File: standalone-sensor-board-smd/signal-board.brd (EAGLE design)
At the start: 26 x 93.5 mm, 27 parts, among them IC2 HEF4051BT,653, J1 sensors, J3 to_next_board, J4 to_controller

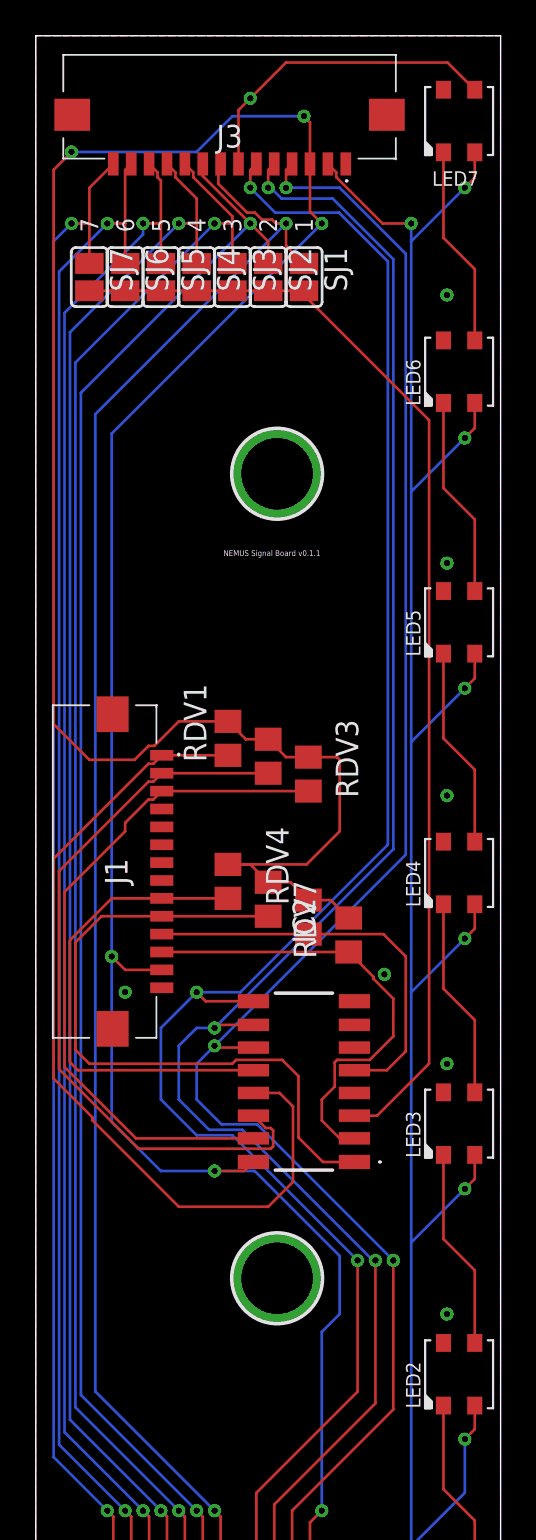
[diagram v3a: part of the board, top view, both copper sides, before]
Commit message: tidy silk screen
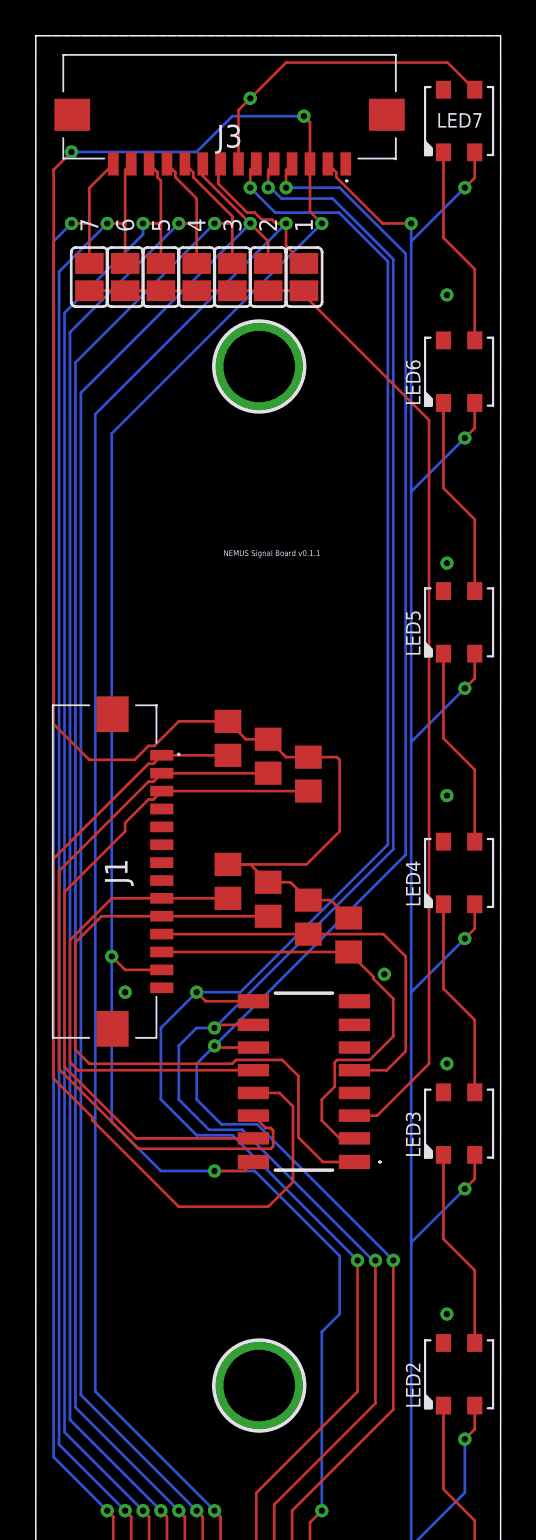
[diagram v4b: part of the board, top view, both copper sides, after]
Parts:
- moved U$1 6.08 mm to (12.5, 75.0)
- moved U$2 6.08 mm to (12.5, 18.0)
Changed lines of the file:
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@@
 <elements>
 <element name="SJ1" library="jumper" library_urn="urn:adsk.eagle:library:252" package="SJ" package3d_urn="urn:adsk.eagle:package:15471/1" value="" x="15" y="80" smashed="yes" rot="R270">
-<attribute name="NAME" x="16.143" y="81.651" size="1.27" layer="25" ratio="10" rot="R270"/>
 <attribute name="POPULARITY" value="33" x="15" y="80" size="1.778" layer="27" rot="R270" display="off"/>
 <attribute name="VALUE" x="15" y="79.5999" size="0.02" layer="27" rot="R270"/>
 </element>
 <element name="SJ2" library="jumper" library_urn="urn:adsk.eagle:library:252" package="SJ" package3d_urn="urn:adsk.eagle:package:15471/1" value="" x="13" y="80" smashed="yes" rot="R270">
-<attribute name="NAME" x="14.143" y="81.651" size="1.27" layer="25" ratio="10" rot="R270"/>
 <attribute name="POPULARITY" value="33" x="13" y="80" size="1.778" layer="27" rot="R270" display="off"/>
 <attribute name="VALUE" x="13" y="79.5999" size="0.02" layer="27" rot="R270"/>
 </element>
 <element name="SJ3" library="jumper" library_urn="urn:adsk.eagle:library:252" package="SJ" package3d_urn="urn:adsk.eagle:package:15471/1" value="" x="11" y="80" smashed="yes" rot="R270">
-<attribute name="NAME" x="12.143" y="81.651" size="1.27" layer="25" ratio="10" rot="R270"/>
 <attribute name="POPULARITY" value="33" x="11" y="80" size="1.778" layer="27" rot="R270" display="off"/>
 <attribute name="VALUE" x="11" y="79.5999" size="0.02" layer="27" rot="R270"/>
 </element>
 <element name="SJ4" library="jumper" library_urn="urn:adsk.eagle:library:252" package="SJ" package3d_urn="urn:adsk.eagle:package:15471/1" value="" x="9" y="80" smashed="yes" rot="R270">
-<attribute name="NAME" x="10.143" y="81.651" size="1.27" layer="25" ratio="10" rot="R270"/>
 <attribute name="POPULARITY" value="33" x="9" y="80" size="1.778" layer="27" rot="R270" display="off"/>
 <attribute name="VALUE" x="9" y="79.5999" size="0.02" layer="27" rot="R270"/>
 </element>
 <element name="SJ5" library="jumper" library_urn="urn:adsk.eagle:library:252" package="SJ" package3d_urn="urn:adsk.eagle:package:15471/1" value="" x="7" y="80" smashed="yes" rot="R270">
-<attribute name="NAME" x="8.143" y="81.651" size="1.27" layer="25" ratio="10" rot="R270"/>
 <attribute name="POPULARITY" value="33" x="7" y="80" size="1.778" layer="27" rot="R270" display="off"/>
 <attribute name="VALUE" x="7" y="79.5999" size="0.02" layer="27" rot="R270"/>
 </element>
 <element name="SJ6" library="jumper" library_urn="urn:adsk.eagle:library:252" package="SJ" package3d_urn="urn:adsk.eagle:package:15471/1" value="" x="5" y="80" smashed="yes" rot="R270">
-<attribute name="NAME" x="6.143" y="81.651" size="1.27" layer="25" ratio="10" rot="R270"/>
 <attribute name="POPULARITY" value="33" x="5" y="80" size="1.778" layer="27" rot="R270" display="off"/>
 <attribute name="VALUE" x="5" y="79.5999" size="0.02" layer="27" rot="R270"/>
 </element>
 <element name="SJ7" library="jumper" library_urn="urn:adsk.eagle:library:252" package="SJ" package3d_urn="urn:adsk.eagle:package:15471/1" value="" x="3" y="80" smashed="yes" rot="R270">
-<attribute name="NAME" x="4.143" y="81.651" size="1.27" layer="25" ratio="10" rot="R270"/>
 <attribute name="POPULARITY" value="33" x="3" y="80" size="1.778" layer="27" rot="R270" display="off"/>
 <attribute name="VALUE" x="3" y="79.5999" size="0.02" layer="27" rot="R270"/>
@@
 <attribute name="MOUSER_PRICE-STOCK" value="https://www.mouser.co.uk/ProductDetail/Wurth-Elektronik/686114148922?qs=a9WhcLg8qCz0mPj5zZqo5g%3D%3D" x="4" y="46.75" size="1.778" layer="27" rot="R270" display="off"/>
 <attribute name="NAME" x="4.5" y="46.75" size="1.27" layer="25" rot="R270" align="center"/>
-<attribute name="VALUE" x="4.5" y="46.75" size="1.27" layer="27" rot="R270" align="center"/>
+<attribute name="VALUE" x="2.5" y="46.75" size="1.27" layer="27" rot="R270" align="center"/>
 </element>
 <element name="J3" library="686114148922" package="686114148922" value="to_next_board" x="10.84" y="89.38" smashed="yes" rot="R180">
@@
 </element>
 <element name="RDV1" library="rcl" library_urn="urn:adsk.eagle:library:334" package="R0805" package3d_urn="urn:adsk.eagle:package:23553/2" value="100k" x="10.75" y="54.2" smashed="yes" rot="R270">
-<attribute name="NAME" x="8.274" y="57.248" size="1.27" layer="25" ratio="10" rot="R270"/>
 <attribute name="POPULARITY" value="86" x="10.75" y="54.2" size="1.778" layer="27" rot="R270" display="off"/>
 <attribute name="SPICEPREFIX" value="R" x="10.75" y="54.2" size="1.778" layer="27" rot="R270" display="off"/>
-<attribute name="VALUE" x="10.115" y="56.4606" size="1.27" layer="27" ratio="10" rot="R270"/>
 </element>
 <element name="RDV2" library="rcl" library_urn="urn:adsk.eagle:library:334" package="R0805" package3d_urn="urn:adsk.eagle:package:23553/2" value="100k" x="13" y="53.2" smashed="yes" rot="R270">
 <attribute name="POPULARITY" value="86" x="13" y="53.2" size="1.778" layer="27" rot="R270" display="off"/>
 <attribute name="SPICEPREFIX" value="R" x="13" y="53.2" size="1.778" layer="27" rot="R270" display="off"/>
-<attribute name="VALUE" x="12.365" y="55.4606" size="1.27" layer="27" ratio="10" rot="R270"/>
 </element>
 <element name="RDV3" library="rcl" library_urn="urn:adsk.eagle:library:334" package="R0805" package3d_urn="urn:adsk.eagle:package:23553/2" value="100k" x="15.25" y="52.2" smashed="yes" rot="R270">
-<attribute name="NAME" x="16.774" y="55.248" size="1.27" layer="25" ratio="10" rot="R270"/>
 <attribute name="POPULARITY" value="86" x="15.25" y="52.2" size="1.778" layer="27" rot="R270" display="off"/>
 <attribute name="SPICEPREFIX" value="R" x="15.25" y="52.2" size="1.778" layer="27" rot="R270" display="off"/>
-<attribute name="VALUE" x="14.615" y="54.4606" size="1.27" layer="27" ratio="10" rot="R270"/>
 </element>
 <element name="RDV4" library="rcl" library_urn="urn:adsk.eagle:library:334" package="R0805" package3d_urn="urn:adsk.eagle:package:23553/2" value="100k" x="10.75" y="46.2" smashed="yes" rot="R270">
-<attribute name="NAME" x="12.874" y="49.248" size="1.27" layer="25" ratio="10" rot="R270"/>
 <attribute name="POPULARITY" value="86" x="10.75" y="46.2" size="1.778" layer="27" rot="R270" display="off"/>
 <attribute name="SPICEPREFIX" value="R" x="10.75" y="46.2" size="1.778" layer="27" rot="R270" display="off"/>
-<attribute name="VALUE" x="10.115" y="48.4606" size="1.27" layer="27" ratio="10" rot="R270"/>
 </element>
 <element name="RDV5" library="rcl" library_urn="urn:adsk.eagle:library:334" package="R0805" package3d_urn="urn:adsk.eagle:package:23553/2" value="100k" x="13" y="45.2" smashed="yes" rot="R270">
 <attribute name="POPULARITY" value="86" x="13" y="45.2" size="1.778" layer="27" rot="R270" display="off"/>
 <attribute name="SPICEPREFIX" value="R" x="13" y="45.2" size="1.778" layer="27" rot="R270" display="off"/>
-<attribute name="VALUE" x="12.365" y="47.4606" size="1.27" layer="27" ratio="10" rot="R270"/>
 </element>
 <element name="RDV6" library="rcl" library_urn="urn:adsk.eagle:library:334" package="R0805" package3d_urn="urn:adsk.eagle:package:23553/2" value="100k" x="15.25" y="44.2" smashed="yes" rot="R270">
 <attribute name="POPULARITY" value="86" x="15.25" y="44.2" size="1.778" layer="27" rot="R270" display="off"/>
 <attribute name="SPICEPREFIX" value="R" x="15.25" y="44.2" size="1.778" layer="27" rot="R270" display="off"/>
-<attribute name="VALUE" x="14.615" y="46.4606" size="1.27" layer="27" ratio="10" rot="R270"/>
 </element>
 <element name="RDV7" library="rcl" library_urn="urn:adsk.eagle:library:334" package="R0805" package3d_urn="urn:adsk.eagle:package:23553/2" value="100k" x="17.5" y="43.2" smashed="yes" rot="R270">
-<attribute name="NAME" x="14.424" y="46.248" size="1.27" layer="25" ratio="10" rot="R270"/>
 <attribute name="POPULARITY" value="86" x="17.5" y="43.2" size="1.778" layer="27" rot="R270" display="off"/>
 <attribute name="SPICEPREFIX" value="R" x="17.5" y="43.2" size="1.778" layer="27" rot="R270" display="off"/>
-<attribute name="VALUE" x="16.865" y="45.4606" size="1.27" layer="27" ratio="10" rot="R270"/>
 </element>
 <element name="LED1" library="adafruit" package="LED3535" value="WS2812B3535" x="23.68" y="4.61" smashed="yes" rot="R90">
@@
 </element>
 <element name="LED7" library="adafruit" package="LED3535" value="WS2812B3535" x="23.68" y="88.73" smashed="yes" rot="R90">
-<attribute name="NAME" x="24.775" y="85.921" size="0.8128" layer="25" ratio="18" rot="R180"/>
+<attribute name="NAME" x="25.025" y="89.171" size="0.8128" layer="25" ratio="18" rot="R180"/>
 </element>
 <element name="IC2" library="HEF4051BT_653" package="HEF4051BT653" value="HEF4051BT,653" x="15" y="35" smashed="yes" rot="R90">
@@
 <attribute name="MOUSER_PART_NUMBER" value="771-HEF4051BTD-T" x="15" y="35" size="1.778" layer="27" rot="R90" display="off"/>
 <attribute name="MOUSER_PRICE-STOCK" value="https://www.mouser.co.uk/ProductDetail/Nexperia/HEF4051BT653?qs=me8TqzrmIYWoNumSZf8zVw%3D%3D" x="15" y="35" size="1.778" layer="27" rot="R90" display="off"/>
-<attribute name="NAME" x="15" y="44" size="1.27" layer="25" rot="R90" align="center"/>
-<attribute name="VALUE" x="13" y="49" size="1.27" layer="27" rot="R90" align="center"/>
 </element>
-<element name="U$2" library="microbuilder" package="MICROBUILDER_MOUNTINGHOLE_4.0_PLATEDTHIN" value="MICROBUILDER_MOUNTINGHOLEMICROBUILDER_MOUNTINGHOL_4.0" x="13.5" y="24" smashed="yes"/>
-<element name="U$1" library="microbuilder" package="MICROBUILDER_MOUNTINGHOLE_4.0_PLATEDTHIN" value="MICROBUILDER_MOUNTINGHOLEMICROBUILDER_MOUNTINGHOL_4.0" x="13.5" y="69" smashed="yes"/>
+<element name="U$2" library="microbuilder" package="MICROBUILDER_MOUNTINGHOLE_4.0_PLATEDTHIN" value="MICROBUILDER_MOUNTINGHOLEMICROBUILDER_MOUNTINGHOL_4.0" x="12.5" y="18" smashed="yes"/>
+<element name="U$1" library="microbuilder" package="MICROBUILDER_MOUNTINGHOLE_4.0_PLATEDTHIN" value="MICROBUILDER_MOUNTINGHOLEMICROBUILDER_MOUNTINGHOL_4.0" x="12.5" y="75" smashed="yes"/>
 </elements>
 <signals>
